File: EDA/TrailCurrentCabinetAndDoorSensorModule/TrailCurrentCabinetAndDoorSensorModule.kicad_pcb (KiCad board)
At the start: 2 copper layers, 56.4 x 64.2 mm, 12 parts, among them J1 DHT22, U1 Amazon Buck Converter, U2 ESP32-C6-Super-Mini, U3 SN65HVD230, U4 ZX-XH2.54-4PWT

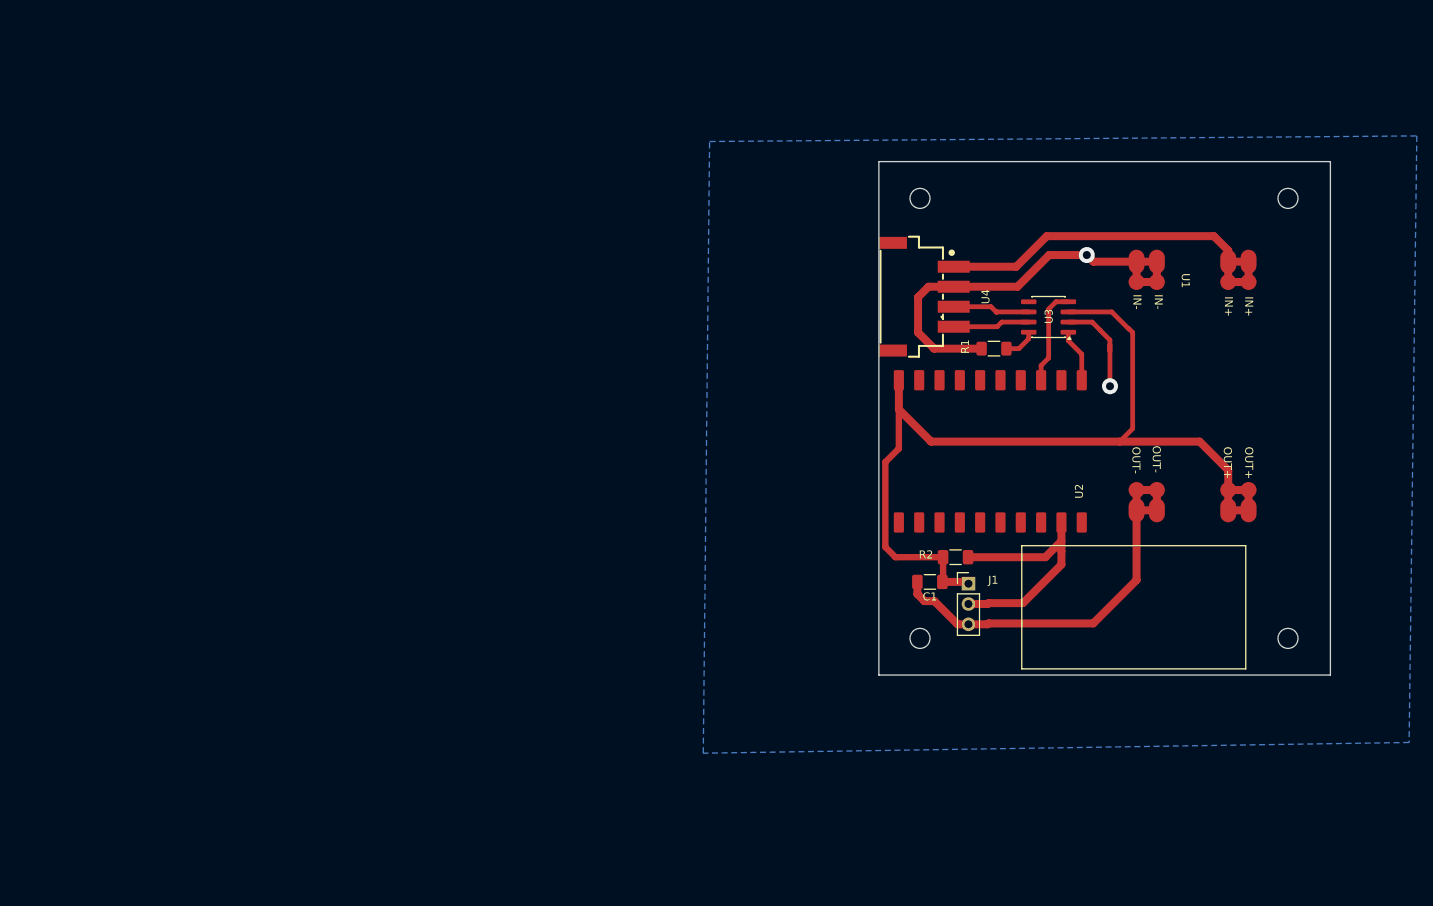
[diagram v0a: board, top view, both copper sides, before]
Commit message: Firmware added. Schematic added. CAD files started.
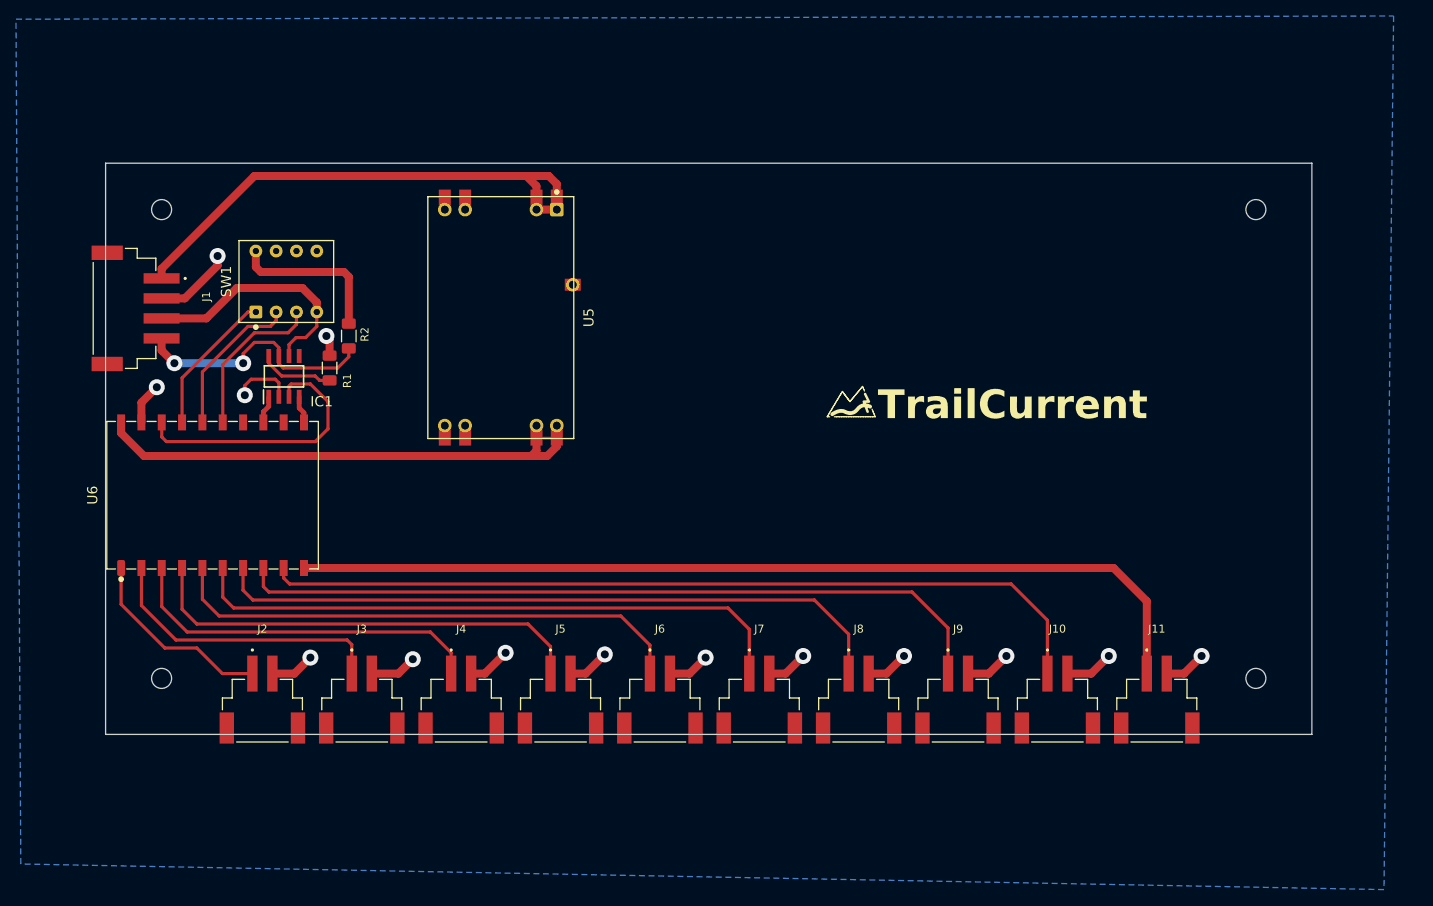
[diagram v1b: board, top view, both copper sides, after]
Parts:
- removed C1: 100nF, Capacitor_SMD:C_1206_3216Metric_Pad1.33x1.80mm_HandSolder
- removed H1, H2, H3, H4: MountingHole, MountingHole:MountingHole_2.5mm
- removed U1: Amazon Buck Converter, Converter_DCDC:AmazonBuckConverter
- removed U2: ESP32-C6-Super-Mini, RF_Module:ESP32-C6-Super-Mini
- removed U3: SN65HVD230, Package_SO:SOIC-8_3.9x4.9mm_P1.27mm
- removed U4: ZX-XH2.54-4PWT, easyeda2kicad:CONN-SMD_4P-P2.50-WAFER-254W-4P
- added IC1: SN65HVD230DR, TrailCurrentFootprints:SN65HVD230DR, F.Cu at (52.5, 87.2)
- added J10: S2B-XH-SM4-TB, TrailCurrentFootprints:JST_S2B-XH-SM4-TB, F.Cu at (149.2, 131.2)
- added J11: S2B-XH-SM4-TB, TrailCurrentFootprints:JST_S2B-XH-SM4-TB, F.Cu at (161.6, 131.2)
- added J2: S2B-XH-SM4-TB, TrailCurrentFootprints:JST_S2B-XH-SM4-TB, F.Cu at (49.8, 131.2)
- added J3: S2B-XH-SM4-TB, TrailCurrentFootprints:JST_S2B-XH-SM4-TB, F.Cu at (62.2, 131.2)
- added J4: S2B-XH-SM4-TB, TrailCurrentFootprints:JST_S2B-XH-SM4-TB, F.Cu at (74.6, 131.2)
- added J5: S2B-XH-SM4-TB, TrailCurrentFootprints:JST_S2B-XH-SM4-TB, F.Cu at (87.1, 131.2)
- added J6: S2B-XH-SM4-TB, TrailCurrentFootprints:JST_S2B-XH-SM4-TB, F.Cu at (99.5, 131.2)
- added J7: S2B-XH-SM4-TB, TrailCurrentFootprints:JST_S2B-XH-SM4-TB, F.Cu at (111.9, 131.2)
- added J8: S2B-XH-SM4-TB, TrailCurrentFootprints:JST_S2B-XH-SM4-TB, F.Cu at (124.3, 131.2)
- added J9: S2B-XH-SM4-TB, TrailCurrentFootprints:JST_S2B-XH-SM4-TB, F.Cu at (136.8, 131.2)
- added LOGO: TrailCurrentLogo_Text, TrailCurrentFootprints:TrailCurrentLogo_Text, F.Cu at (143.6, 90.8)
- added LOGO: TrailCurrentLogo_Icon, TrailCurrentFootprints:TrailCurrentLogo_Icon, F.Cu at (123.4, 90.4)
- added SW1: DS-04, TrailCurrentFootprints:DS-04, F.Cu at (52.8, 75.4)
- added U5: Mini560, TrailCurrentFootprints:Mini560, F.Cu at (79.6, 79.9)
- added U6: ESP32-C6-SuperMini, TrailCurrentFootprints:ESP32-C6-SuperMini_SMD, F.Cu at (43.6, 102.1)
- J1: value DHT22 -> S4B-XH-SM4-TB; footprint Connector_PinHeader_2.54mm:PinHeader_1x03_P2.54mm_Vertical -> TrailCurrentFootprints:JST_S4B-XH-SM4-TB
- R2: value 4.7K -> 120; footprint Capacitor_SMD:C_1206_3216Metric_Pad1.33x1.80mm_HandSolder -> Resistor_SMD:R_1206_3216Metric_Pad1.30x1.75mm_HandSolder
- moved J1 113.0 mm to (30.4, 78.8), turned to -90 degrees
- moved R1 83.1 mm to (58.2, 86.2), turned to -90 degrees
- moved R2 80.7 mm to (60.6, 82.2), turned to 90 degrees
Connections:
- J1 pad 1: +3.3V -> +12V
- J1 pad 2: DHT_READING -> GND
- J1 pad 3: GND -> CANL
- R2 pad 1: +3.3V -> CANH
- R2 pad 2: DHT_READING -> Net-(R2-Pad2)
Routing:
- net RSW10: track 0.00 -> 116.1 mm
- net RSW09: track 0.00 -> 105.6 mm
- net RSW08: track 0.00 -> 95.7 mm
- net RSW07: track 0.00 -> 85.7 mm
- net +3.3V: track 116.4 -> 34.1 mm
- net RSW06: track 0.00 -> 76.7 mm
- net RSW05: track 0.00 -> 65.8 mm
- net +5V: track 0.00 -> 63.7 mm
- net RSW04: track 0.00 -> 56.5 mm
- net RSW03: track 0.00 -> 46.0 mm
- net GND: track 118.5 -> 80.4 mm, vias 2 -> 14
- net RSW02: track 0.00 -> 36.6 mm
- net DHT_READING: track 32.7 -> 0.00 mm
- net RSW01: track 0.00 -> 24.5 mm
- net CANH: track 9.61 -> 31.5 mm, vias 0 -> 2
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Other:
- board size 56.4 x 64.2 mm -> 150.8 x 71.4 mm
